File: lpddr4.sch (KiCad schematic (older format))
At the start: 96 parts, among them U1 MT53D1024M32D4DT-053, U3 MT53D1024M32D4DT-053

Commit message: Updated LPDDR4. Fixed reversed clocks
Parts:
- removed R100, R102, R46, R48: R_0R_0402, arvsom-footprints:0402-res, symbol arvsom:R_0R_0402
- removed R101, R43, R47, R98: R_10k_0402, arvsom-footprints:0402-res, symbol arvsom:R_10k_0402
- added R? (x2): R_10k_0402, arvsom-footprints:0402-res, symbol arvsom:R_10k_0402
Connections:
- net VDDQ is gone; now on net VCC_1V1: C208.1, C211.1, C213.1, C214.1, C217.1, C219.1, C222.1, C224.1, C227.1, C229.1, C232.1, C234.1, C237.1, C239.1, C71.1, C72.1, C74.1, C75.1, C77.1, C78.1, C80.1, C81.1, C83.1, C84.1, C86.1, C87.1, C89.1, C91.1, R103.1, R106.1, R42.2, R44.1, R45.2, R94.1, R97.2, R99.2, U1.AA10 (VDDQ), U1.AA3 (VDDQ), U1.AA5 (VDDQ), U1.AA8 (VDDQ), U1.B10 (VDDQ), U1.B3 (VDDQ), U1.B5 (VDDQ), U1.B8 (VDDQ), U1.D1 (VDDQ), U1.D12 (VDDQ), U1.D5 (VDDQ), U1.D8 (VDDQ), U1.F10 (VDDQ), U1.F3 (VDDQ), U1.U10 (VDDQ), U1.U3 (VDDQ), U1.W1 (VDDQ), U1.W12 (VDDQ), U1.W5 (VDDQ), U1.W8 (VDDQ), U3.AA10 (VDDQ), U3.AA3 (VDDQ), U3.AA5 (VDDQ), U3.AA8 (VDDQ), U3.B10 (VDDQ), U3.B3 (VDDQ), U3.B5 (VDDQ), U3.B8 (VDDQ), U3.D1 (VDDQ), U3.D12 (VDDQ), U3.D5 (VDDQ), U3.D8 (VDDQ), U3.F10 (VDDQ), U3.F3 (VDDQ), U3.U10 (VDDQ), U3.U3 (VDDQ), U3.W1 (VDDQ), U3.W12 (VDDQ), U3.W5 (VDDQ), U3.W8 (VDDQ)
- net DDR0_CK0_N: now also U1.J9 (CK_C_A); no longer U1.J8 (CK_T_A)
- net DDR0_CK0_P: now also U1.J8 (CK_T_A); no longer U1.J9 (CK_C_A)
- net DDR0_CK1_N: now also U1.P9 (CK_C_B); no longer U1.P8 (CK_T_B)
- net DDR0_CK1_P: now also U1.P8 (CK_T_B); no longer U1.P9 (CK_C_B)
- net DDR0_DQS0N: now also U1.E3 (DQS0_C_A); no longer U1.D3 (DQS0_T_A)
- net DDR0_DQS0P: now also U1.D3 (DQS0_T_A); no longer U1.E3 (DQS0_C_A)
- net DDR0_DQS1N: now also U1.E10 (DQS1_C_A); no longer U1.D10 (DQS1_T_A)
- net DDR0_DQS1P: now also U1.D10 (DQS1_T_A); no longer U1.E10 (DQS1_C_A)
- net DDR0_DQS2N: now also U1.V3 (DQS0_C_B); no longer U1.W3 (DQS0_T_B)
- net DDR0_DQS2P: now also U1.W3 (DQS0_T_B); no longer U1.V3 (DQS0_C_B)
- net DDR0_DQS3N: now also U1.V10 (DQS1_C_B); no longer U1.W10 (DQS1_T_B)
- net DDR0_DQS3P: now also U1.W10 (DQS1_T_B); no longer U1.V10 (DQS1_C_B)
- net DDR0_ODT1: now also R44.2, R93.2
- net DDR0_ODT_0: now also U1.G2 (ODT_CA_A), R?.1
- net DDR0_ODT_1: now also R?.2; no longer R44.2, R93.2
- net DDR0_RSTN: now also U1.T11 (RESET_N)
- net DDR1_CK0_N: now also U3.J9 (CK_C_A); no longer U3.J8 (CK_T_A)
- net DDR1_CK0_P: now also U3.J8 (CK_T_A); no longer U3.J9 (CK_C_A)
- net DDR1_CK1_N: now also U3.P9 (CK_C_B); no longer U3.P8 (CK_T_B)
- net DDR1_CK1_P: now also U3.P8 (CK_T_B); no longer U3.P9 (CK_C_B)
- net DDR1_DQS0N: now also U3.E3 (DQS0_C_A); no longer U3.D3 (DQS0_T_A)
- net DDR1_DQS0P: now also U3.D3 (DQS0_T_A); no longer U3.E3 (DQS0_C_A)
- net DDR1_DQS1N: now also U3.E10 (DQS1_C_A); no longer U3.D10 (DQS1_T_A)
- net DDR1_DQS1P: now also U3.D10 (DQS1_T_A); no longer U3.E10 (DQS1_C_A)
- net DDR1_DQS2N: now also U3.V3 (DQS0_C_B); no longer U3.W3 (DQS0_T_B)
- net DDR1_DQS2P: now also U3.W3 (DQS0_T_B); no longer U3.V3 (DQS0_C_B)
- net DDR1_DQS3N: now also U3.V10 (DQS1_C_B); no longer U3.W10 (DQS1_T_B)
- net DDR1_DQS3P: now also U3.W10 (DQS1_T_B); no longer U3.V10 (DQS1_C_B)
- net DDR1_ODT0: now also R104.1; no longer R107.1
- net DDR1_ODT1: now also R106.2, R107.1, R108.2; no longer R104.1
- net DDR1_ODT_0: now also R103.2, R104.2, R105.2, U3.G2 (ODT_CA_A), R?.1; no longer R106.2, R107.2, R108.2
- net DDR1_ODT_1: now also R107.2, R?.2; no longer R103.2, R104.2, R105.2
- net DDR1_RSTN: now also U3.T11 (RESET_N)
- net VDD1 renamed VCC_1V8
- net VDD2 renamed VCC_1V1
- net VCC_1V1: no longer C225.1, C230.1
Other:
- moved on the sheet: C207, C210, C215, C220, C225, C230, C236, C241, C73, C76, C79, C82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

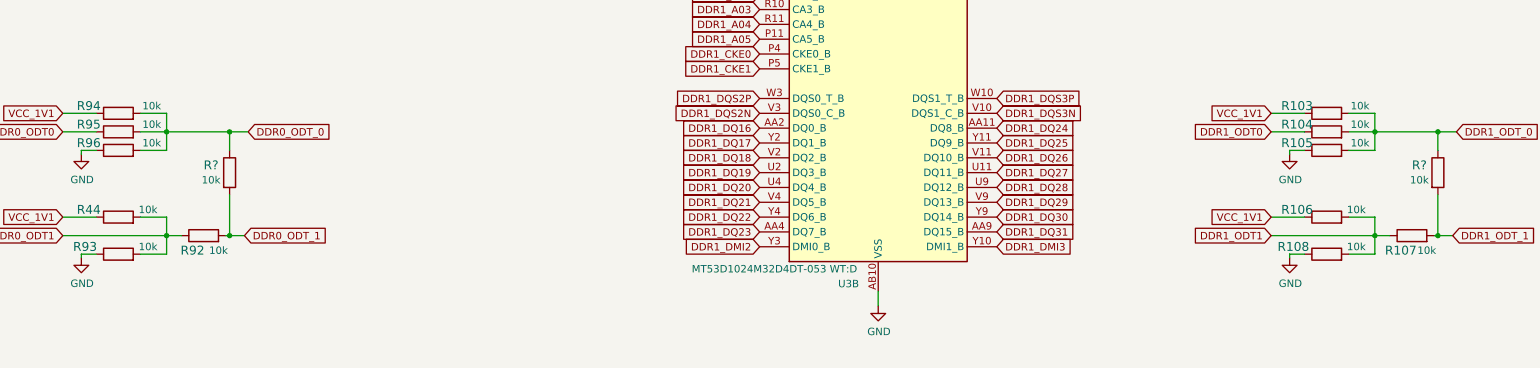
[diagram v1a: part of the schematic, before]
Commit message: Updated VIC config, added reset and crystals
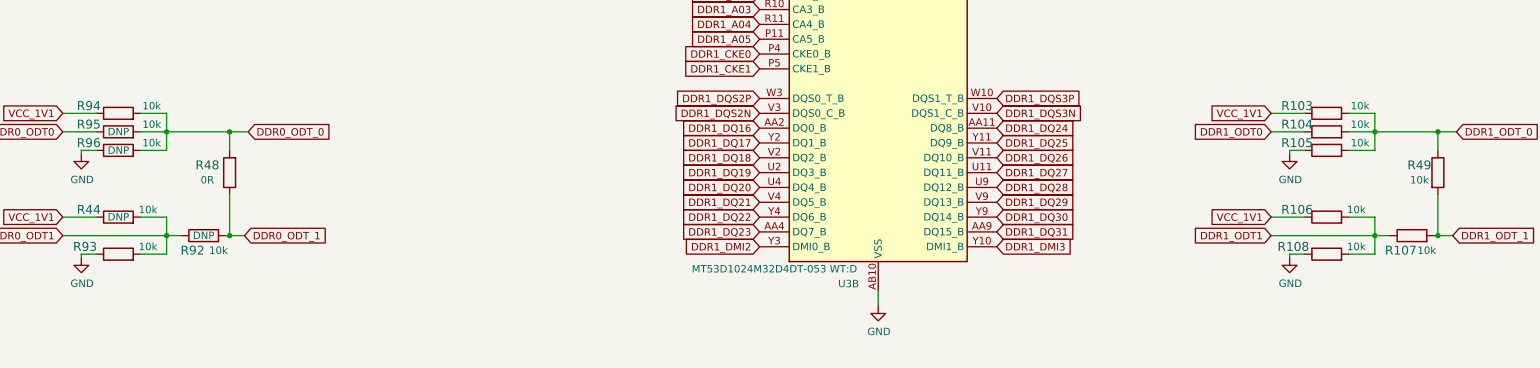
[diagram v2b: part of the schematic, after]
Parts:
- removed R?: R_10k_0402, arvsom-footprints:0402-res, symbol arvsom:R_10k_0402
- added R48: R_0R_0402, arvsom-footprints:0402-res, symbol arvsom:R_0R_0402
- R44, R92, R95, R96: DNP (none) -> DNP
- gave numbers to parts that had none: 1
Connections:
- net DDR0_ODT_0: now also R48.2
- net DDR0_ODT_1: now also R48.1
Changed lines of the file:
@@
 F 5 "CRCW040210K0FKEDHP" H 6625 8800 60  0001 L CNN "MPN"
 F 6 "10k" H 6525 8400 50  0000 C CNN "Val"
+F 7 "DNP" H 6425 8500 50  0000 C CNN "DNP"
 	1    6425 8500
 	1    0    0    -1
@@
 F 5 "CRCW040210K0FKEDHP" H 6050 8675 60  0001 L CNN "MPN"
 F 6 "10k" H 6050 8425 50  0000 C CNN "Val"
+F 7 "DNP" H 5850 8375 50  0000 C CNN "DNP"
 	1    5850 8375
 	1    0    0    -1
@@
 F 5 "CRCW040210K0FKEDHP" H 6050 8100 60  0001 L CNN "MPN"
 F 6 "10k" H 6075 7850 50  0000 C CNN "Val"
+F 7 "DNP" H 5850 7800 50  0000 C CNN "DNP"
 	1    5850 7800
 	1    0    0    -1
@@
 F 5 "CRCW040210K0FKEDHP" H 6050 8225 60  0001 L CNN "MPN"
 F 6 "10k" H 6075 7975 50  0000 C CNN "Val"
+F 7 "DNP" H 5850 7925 50  0000 C CNN "DNP"
 	1    5850 7925
 	1    0    0    -1
@@
 Wire Wire Line
 	6575 8500 6600 8500
-$Comp
-L arvsom:R_10k_0402 R?
-U 1 1 60D63288
-P 6600 8075
-F 0 "R?" V 6550 7950 60  0000 C CNN
-F 1 "R_10k_0402" H 6600 7925 60  0001 C CNN
-F 2 "arvsom-footprints:0402-res" H 6800 8275 60  0001 L CNN
-F 3 "" H 6600 8075 50  0001 C CNN
-F 4 "VISHAY" H 6800 8475 60  0001 L CNN "Manufacturer"
-F 5 "CRCW040210K0FKEDHP" H 6800 8375 60  0001 L CNN "MPN"
-F 6 "10k" V 6650 7950 50  0000 C CNN "Val"
-	1    6600 8075
-	0    1    1    0
-$EndComp
 Wire Wire Line
 	6600 7925 6600 7800
@@
 VCC_1V1
 $Comp
-L arvsom:GND #PWR?
+L arvsom:GND #PWR0124
 U 1 1 60D9210E
 P 13750 7950
-F 0 "#PWR?" H 13750 7700 50  0001 C CNN
+F 0 "#PWR0124" H 13750 7700 50  0001 C CNN
 F 1 "GND" H 13755 7777 50  0000 C CNN
 F 2 "" H 13750 7950 50  0001 C CNN
@@
 	13750 8625 13750 8650
 $Comp
-L arvsom:GND #PWR?
+L arvsom:GND #PWR0126
 U 1 1 60D92120
 P 13750 8650
-F 0 "#PWR?" H 13750 8400 50  0001 C CNN
+F 0 "#PWR0126" H 13750 8400 50  0001 C CNN
 F 1 "GND" H 13755 8477 50  0000 C CNN
 F 2 "" H 13750 8650 50  0001 C CNN
@@
 	14725 8500 14750 8500
 $Comp
-L arvsom:R_10k_0402 R?
+L arvsom:R_10k_0402 R49
 U 1 1 60D9212A
 P 14750 8075
-F 0 "R?" V 14700 7950 60  0000 C CNN
+F 0 "R49" V 14700 7950 60  0000 C CNN
 F 1 "R_10k_0402" H 14750 7925 60  0001 C CNN
 F 2 "arvsom-footprints:0402-res" H 14950 8275 60  0001 L CNN
@@
 Text GLabel 13700 5250 1    50   Input ~ 0
 VCC_1V1
+$Comp
+L arvsom:R_0R_0402 R?
+U 1 1 60C69FD9
+P 6600 8075
+AR Path="/60751C8D/60C69FD9" Ref="R?"  Part="1"
+AR Path="/60A6123C/60C69FD9" Ref="R48"  Part="1"
+F 0 "R48" V 6650 8225 60  0000 C CNN
+F 1 "R_0R_0402" H 6600 7925 60  0001 C CNN
+F 2 "arvsom-footprints:0402-res" H 6800 8275 60  0001 L CNN
+F 3 "" H 6600 8075 50  0001 C CNN
+F 4 "PANASONIC" H 6800 8475 60  0001 L CNN "Manufacturer"
+F 5 "ERJ2GE0R00X" H 6800 8375 60  0001 L CNN "MPN"
+F 6 "0R" V 6550 8225 50  0000 C CNN "Val"
+	1    6600 8075
+	0    -1   -1   0
+$EndComp
 $EndSCHEMATC

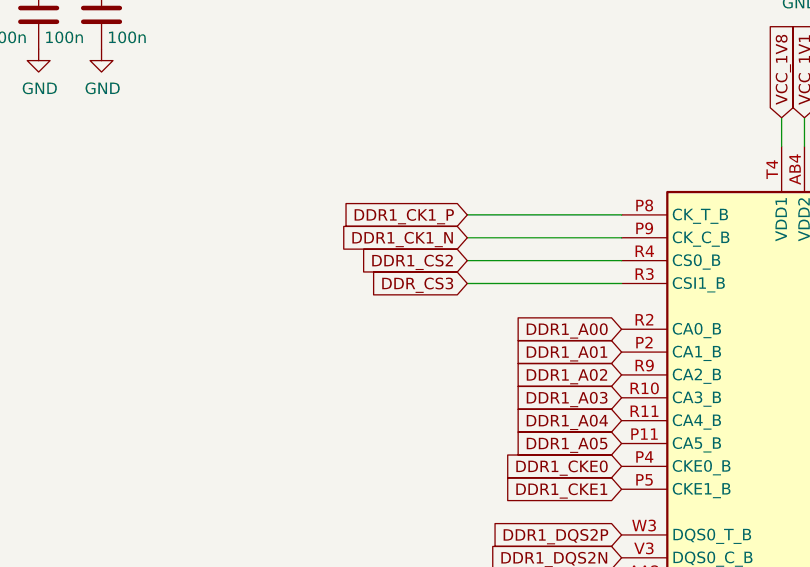
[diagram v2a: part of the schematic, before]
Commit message: Fixed two DDR pinout errors
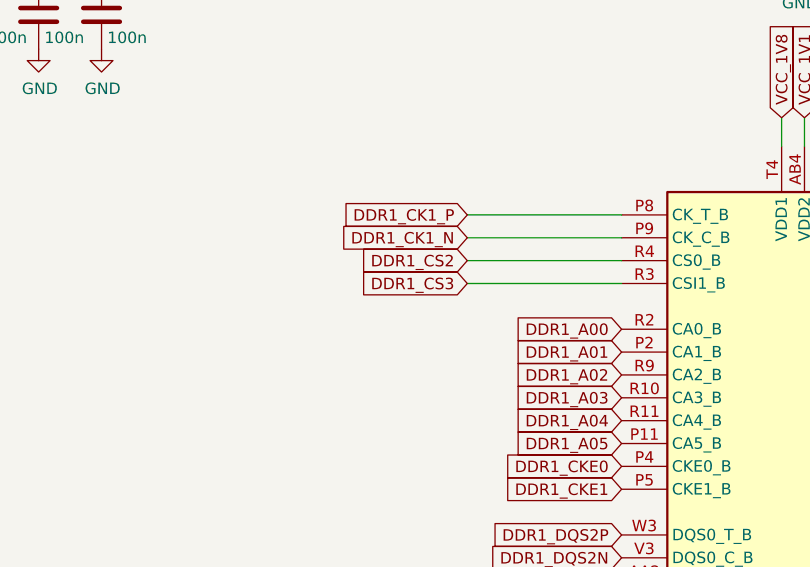
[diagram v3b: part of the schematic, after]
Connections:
- net DDR_CS3 renamed DDR1_CS3
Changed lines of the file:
@@
 DDR1_CKE0
 Text GLabel 9500 6475 0    50   Input ~ 0
-DDR_CS3
+DDR1_CS3
 Text GLabel 9500 6375 0    50   Input ~ 0
 DDR1_CS2
